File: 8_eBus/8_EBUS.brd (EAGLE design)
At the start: 67.4 x 44.8 mm, 20 parts, among them IC1 MCP6542, Q1 BC817, X1 AKL18X-02W, X2 ALLSERIALSLAVE

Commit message: Cleanup, front with lib elements
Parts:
- R5: value 270 -> 180
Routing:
- removed copper zone on layer 1, net N$13
- removed copper zone on layer 16, net N$13
- removed copper zone on layer 1, net N$14
- removed copper zone on layer 16, net N$14
- removed copper zone on layer 1, net N$15
- removed copper zone on layer 16, net N$15
- removed copper zone on layer 16, net N$16
- removed copper zone on layer 1, net N$17
- removed copper zone on layer 16, net N$17
- removed copper zone on layer 1, net N$6
- removed copper zone on layer 16, net N$6
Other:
- board text added: "AllSerial eBus v1.0 42/18"
- board text removed: "AllSerial eBus v1.1 46/18"

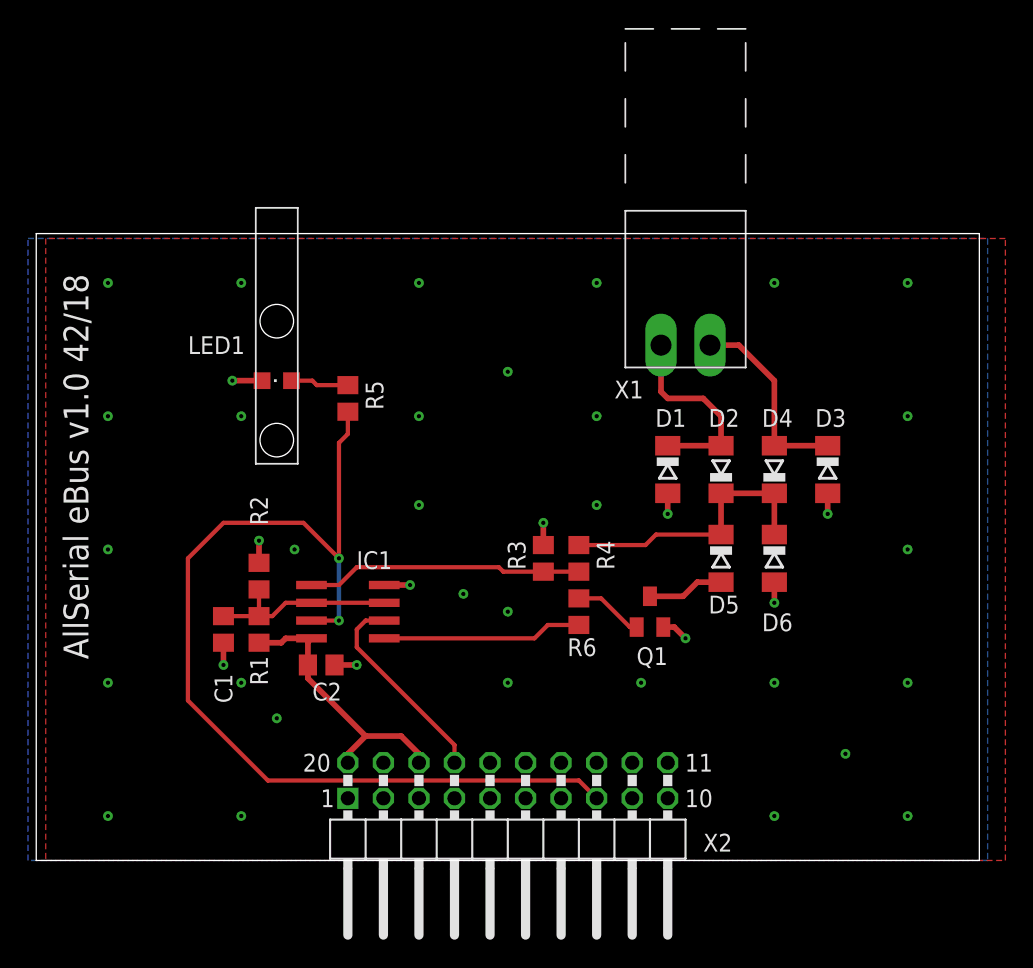
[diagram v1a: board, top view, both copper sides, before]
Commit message: pro mini layout corrected
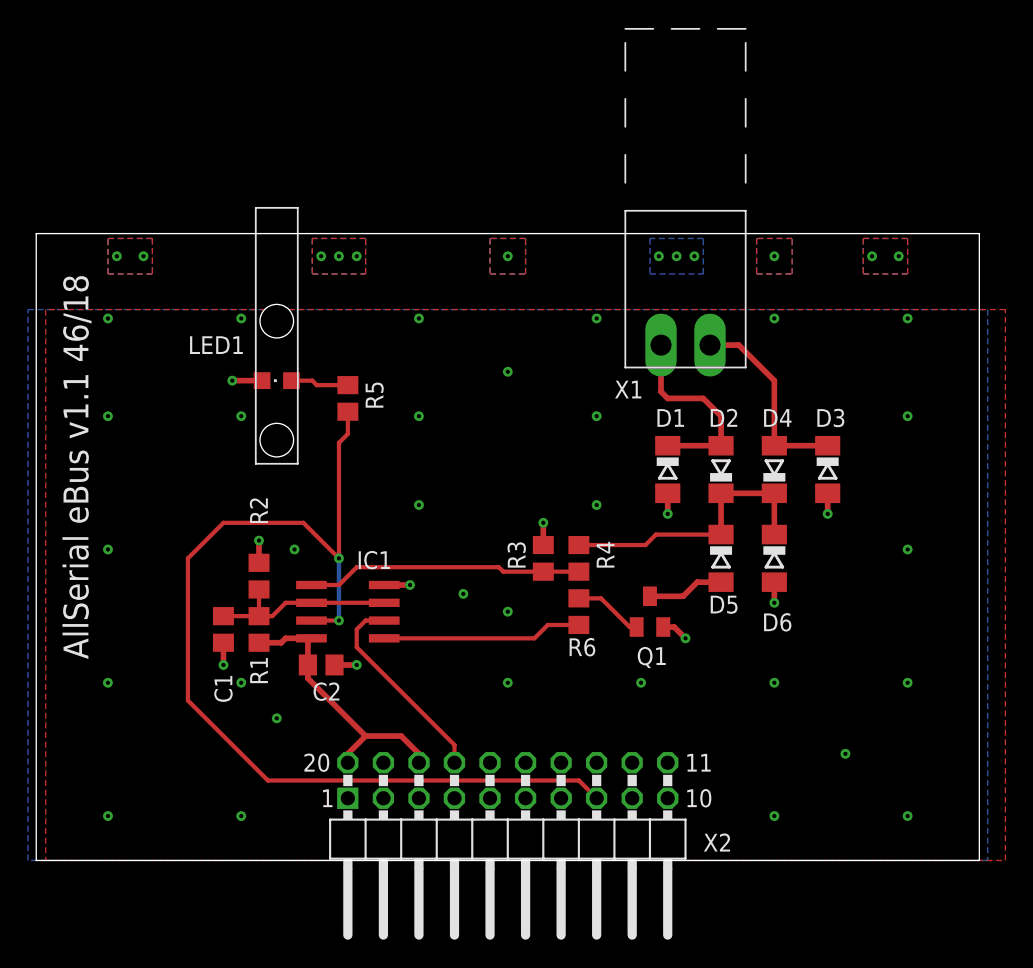
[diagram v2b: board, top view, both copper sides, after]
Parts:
- R5: value 180 -> 270
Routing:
- added copper zone on layer 1, net N$13
- added copper zone on layer 16, net N$13
- added copper zone on layer 1, net N$14
- added copper zone on layer 16, net N$14
- added copper zone on layer 1, net N$15
- added copper zone on layer 16, net N$15
- added copper zone on layer 16, net N$16
- added copper zone on layer 1, net N$17
- added copper zone on layer 16, net N$17
- added copper zone on layer 1, net N$6
- added copper zone on layer 16, net N$6
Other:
- board text added: "AllSerial eBus v1.1 46/18"
- board text removed: "AllSerial eBus v1.0 42/18"
